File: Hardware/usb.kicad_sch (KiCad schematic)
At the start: 8 parts, among them J2 USB_C_Receptacle_USB2.0

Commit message: Finished Boosts and Sensors
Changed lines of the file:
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@@
 (kicad_sch
-	(version 20231120)
+	(version 20250114)
 	(generator "eeschema")
-	(generator_version "8.0")
+	(generator_version "9.0")
 	(paper "A4")
 	(junction
@@
 	(label "Data+"
 		(at 134.62 134.62 90)
-		(fields_autoplaced yes)
 		(effects
 			(font
@@
 	(label "VBUS"
 		(at 129.54 134.62 90)
-		(fields_autoplaced yes)
 		(effects
 			(font
@@
 	(label "Data+"
 		(at 44.45 104.14 0)
-		(fields_autoplaced yes)
 		(effects
 			(font
@@
 	(label "Data-"
 		(at 44.45 99.06 0)
-		(fields_autoplaced yes)
 		(effects
 			(font
@@
 	(label "Data-"
 		(at 132.08 134.62 90)
-		(fields_autoplaced yes)
 		(effects
 			(font
@@
 	(label "Data-"
 		(at 116.84 102.87 0)
-		(fields_autoplaced yes)
 		(effects
 			(font
@@
 	(label "Data+"
 		(at 116.84 107.95 0)
-		(fields_autoplaced yes)
 		(effects
 			(font
@@
 		(shape bidirectional)
 		(at 44.45 99.06 180)
-		(fields_autoplaced yes)
 		(effects
 			(font
@@
 		(shape bidirectional)
 		(at 44.45 104.14 180)
-		(fields_autoplaced yes)
-		(effects
-			(font
+		(effects
+			(font

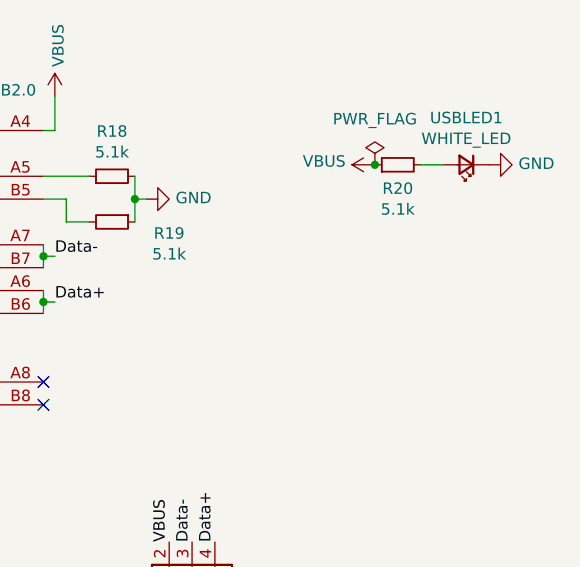
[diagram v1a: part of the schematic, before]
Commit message: Fixed all DRC Errors
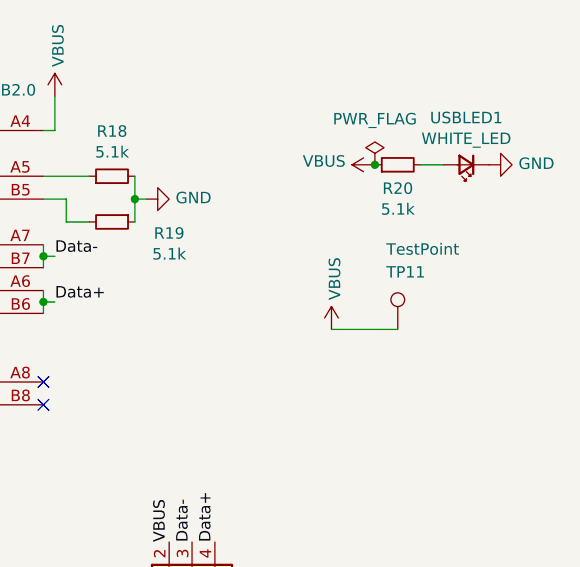
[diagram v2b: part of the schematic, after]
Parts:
- added TP11: TestPoint, TestPoint:TestPoint_Pad_D1.5mm, symbol Connector:TestPoint
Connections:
- net VBUS: now also TP11.1
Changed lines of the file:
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@@
+	(wire
+		(pts
+			(xy 154.94 110.998) (xy 147.574 110.998)
+		)
+		(stroke
+			(width 0)
+			(type default)
+		)
+	)
 	(wire
 		(pts
@@
 					(unit 1)
 				)
+			)
+		)
+	)
+	(symbol
+		(lib_id "power:VBUS")
+		(at 147.574 110.998 0)
+		(unit 1)
+		(exclude_from_sim no)
+		(in_bom yes)
+		(on_board yes)
+		(dnp no)
+		(property "Reference" "#PWR0185"
+			(at 147.574 114.808 0)
+			(effects
+				(font
+					(size 1.27 1.27)
+				)
+				(hide yes)
+			)
+		)
+		(property "Value" "VBUS"
+			(at 147.955 107.7468 90)
+			(effects
+				(font
+					(size 1.27 1.27)
+				)
+				(justify left)
+			)
+		)
+		(property "Footprint" ""
+			(at 147.574 110.998 0)
+			(effects
+				(font
+					(size 1.27 1.27)
+				)
+				(hide yes)
+			)
+		)
+		(property "Datasheet" ""
+			(at 147.574 110.998 0)
+			(effects
+				(font
+					(size 1.27 1.27)
+				)
+				(hide yes)
+			)
+		)
+		(property "Description" ""
+			(at 147.574 110.998 0)
+			(effects
+				(font
+					(size 1.27 1.27)
+				)
+				(hide yes)
+			)
+		)
+		(pin "1"
+		)
+		(instances
+			(project "Ricardo-Stark"
+				(path "/7db990e4-92e1-4f99-b4d2-435bbec1ba83/00000000-0000-0000-0000-000061925999"
+					(reference "#PWR0185")
+					(unit 1)
+				)
+			)
+		)
+	)
+	(symbol
+		(lib_id "Connector:TestPoint")
+		(at 154.94 110.998 0)
+		(unit 1)
+		(exclude_from_sim no)
+		(in_bom yes)
+		(on_board yes)
+		(dnp no)
+		(property "Reference" "TP11"
+			(at 153.67 104.648 0)
+			(effects
+				(font
+					(size 1.27 1.27)
+				)
+				(justify left)
+			)
+		)
+		(property "Value" "TestPoint"
+			(at 153.67 102.1111 0)
+			(effects
+				(font
+					(size 1.27 1.27)
+				)
+				(justify left)
+			)
+		)
+		(property "Footprint" "TestPoint:TestPoint_Pad_D1.5mm"
+			(at 160.02 110.998 0)
+			(effects
+				(font
+					(size 1.27 1.27)
+				)
+				(hide yes)
+			)
+		)
+		(property "Datasheet" "~"
+			(at 160.02 110.998 0)
+			(effects
+				(font
+					(size 1.27 1.27)
+				)
+				(hide yes)
+			)
+		)
+		(property "Description" ""
+			(at 154.94 110.998 0)
+			(effects
+				(font
+					(size 1.27 1.27)
+				)
+				(hide yes)
+			)
+		)
+		(pin "1"
+		)
+		(instances
+			(project "Ricardo-Stark"
+				(path "/7db990e4-92e1-4f99-b4d2-435bbec1ba83/00000000-0000-0000-0000-000061925999"
+					(reference "TP11")
+					(unit 1)
+				)

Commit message: schematic reformatting and bom consolidation
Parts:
- D502: renamed from USBLED1; value WHITE_LED -> LED_WHITE; footprint Resistor_SMD:R_0402_1005Metric -> LED_SMD:LED_0402_1005Metric
- R501: renamed from R18; value 5.1k -> 5.1kΩ
- R502: renamed from R19; value 5.1k -> 5.1kΩ
- R503: renamed from R20; value 5.1k -> 5.1kΩ
- TP501: renamed from TP3; now left out of the parts list
- TP502: renamed from TP4; now left out of the parts list
- TP503: renamed from TP11; now left out of the parts list
- renumbered D2 to D501, J2 to J501
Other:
- moved on the sheet: R503
